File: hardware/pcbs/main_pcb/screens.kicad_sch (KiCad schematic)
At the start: 22 parts, among them J1 Conn_01x02, J2 Conn_01x07, J3 Conn_01x07, J4 Conn_01x13, U1 TXB0104D, U2 TXB0104D, U3 TXB0104D

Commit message: feat(main PCB): Reworks schematic
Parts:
- C1, C2, C3, C4, C5, C6, C7, C8, C9: symbol Device:C -> Lilybrary:Capacitor
- J1: symbol Connector_Generic:Conn_01x02 -> Lilybrary:Conn_01x02
- J2, J3: symbol Connector_Generic:Conn_01x07 -> Lilybrary:Conn_01x07
- J4: symbol Connector_Generic:Conn_01x13 -> Lilybrary:Conn_01x13
- R1: symbol Device:R -> Lilybrary:Resistor
- TP1, TP2, TP3, TP4, TP5: symbol Connector:TestPoint -> Lilybrary:TestPoint
- U1, U2, U3: footprint Package_SO:SOIC-14_3.9x8.7mm_P1.27mm -> Lilibrary:SOIC-14_TXB0104DR; symbol Logic_LevelTranslator:TXB0104D -> Lilybrary:TXB0104DR
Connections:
- net LEFT_EYE_CS-3V3: now also TP1. (1); no longer TP1.1
- net MAIN_SCREEN_CS-3V3: now also TP5. (1); no longer TP5.1
- net MISO_3V3: now also U2.5 (A4); no longer U2.3 (A2)
- net RIGHT_EYE_CS-3V3: now also TP2. (1); no longer TP2.1
- net SCK_3V3: now also U2.3 (A2); no longer U2.2 (A1)
- net SD_CS-3V3: now also TP4. (1); no longer TP4.1
- net DC-3V3 renamed DC_3V3
- net DC_3V3: now also TP3. (1), U2.2 (A1); no longer TP3.1, U2.5 (A4)
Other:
- company: (none) -> Lily's Pad
- title: (none) -> Main PCB: Screens
- moved on the sheet: J1, J2, J3, J4, TP3

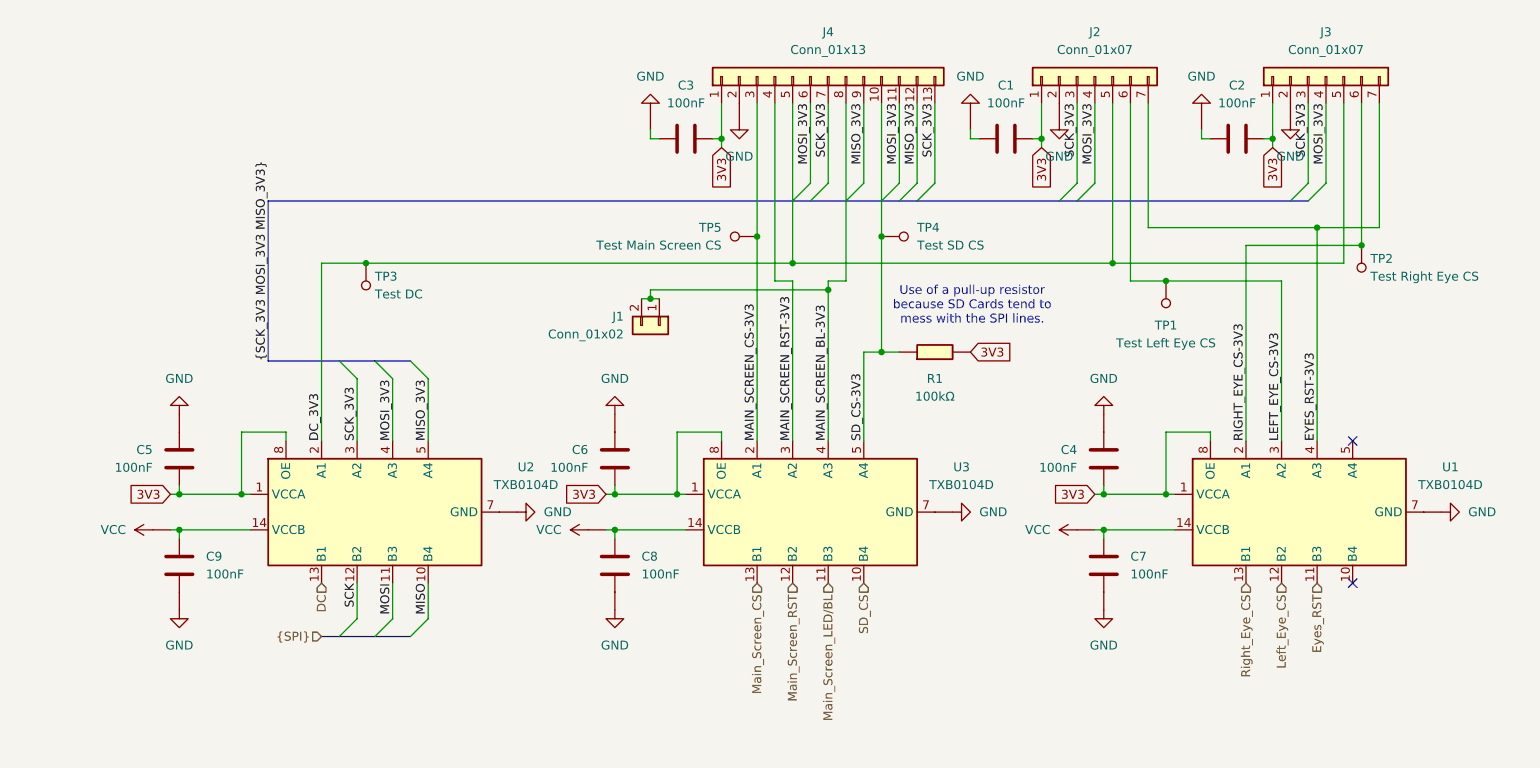
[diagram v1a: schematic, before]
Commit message: feat(main PCB): Removes no longer used BL pin 01x02 header
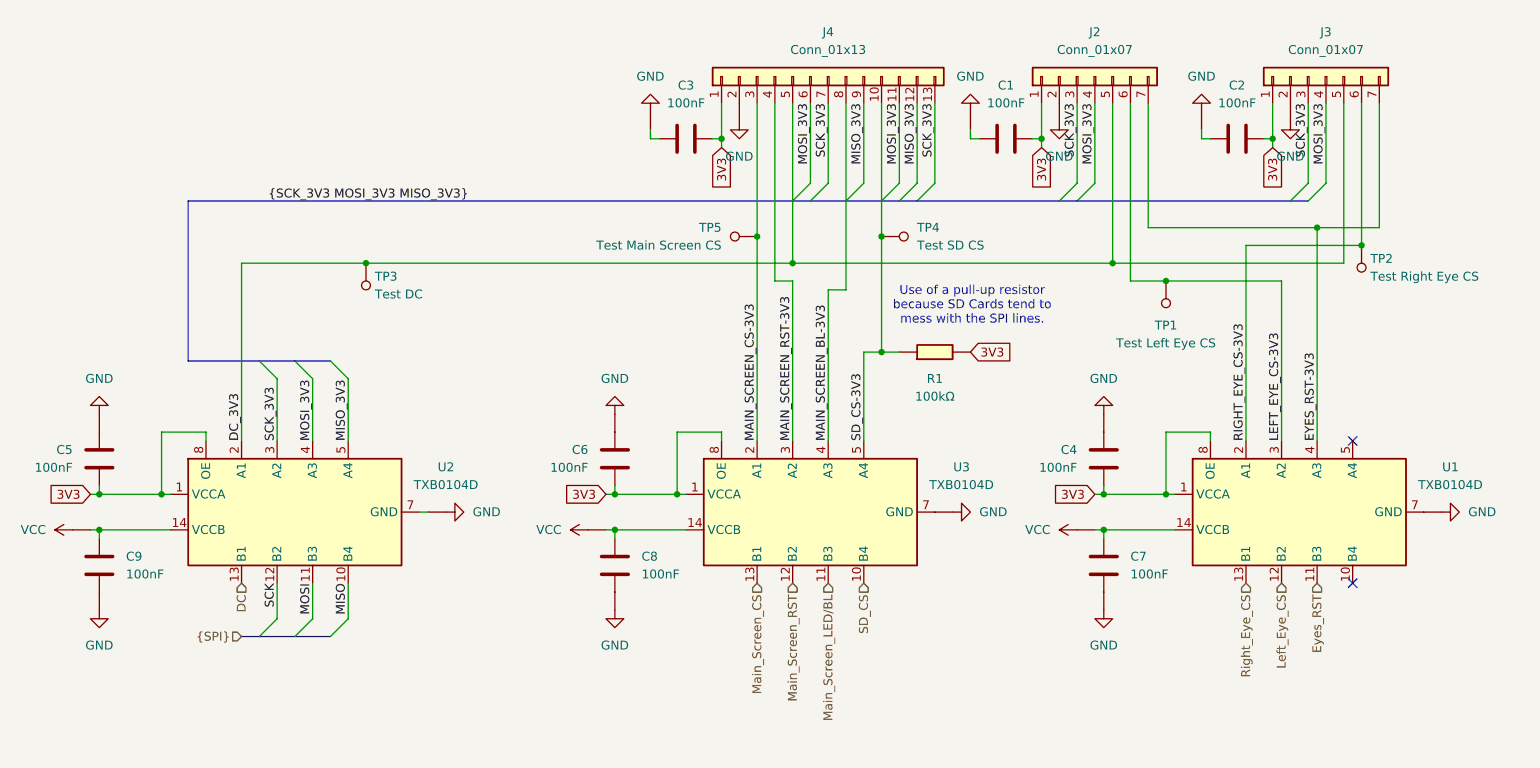
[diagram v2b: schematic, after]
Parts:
- removed J1: Conn_01x02, Lilibrary:JST XH 2 pins, symbol Lilybrary:Conn_01x02
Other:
- moved on the sheet: C5, C9, U2

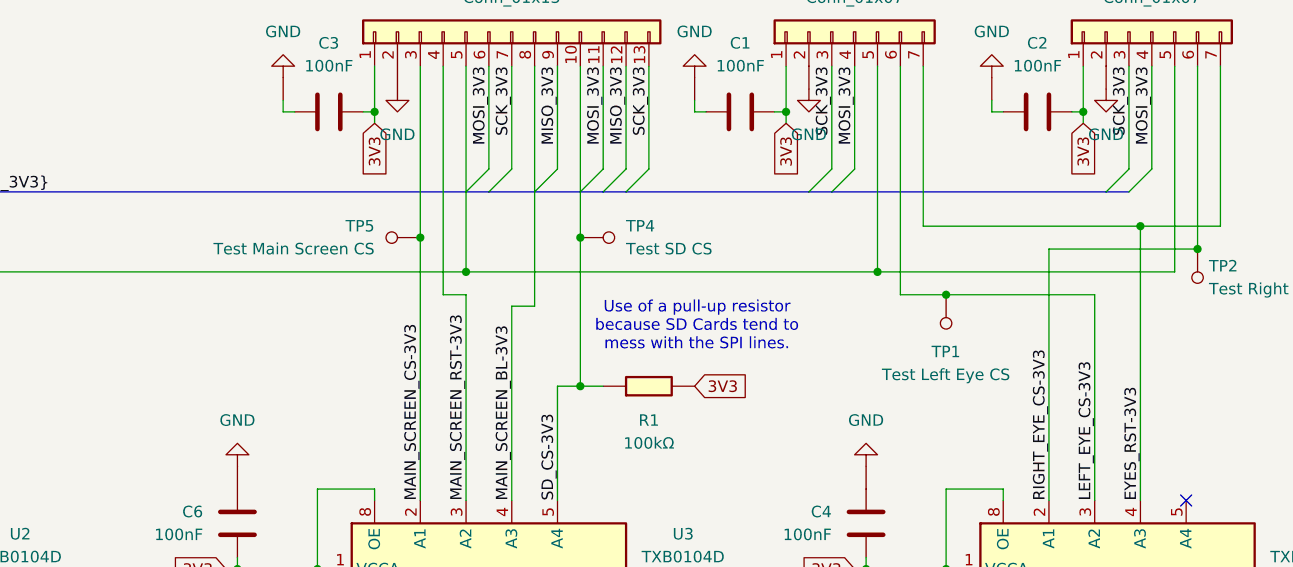
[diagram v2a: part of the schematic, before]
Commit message: feat(main PCB): Fixes main PCB routing issue
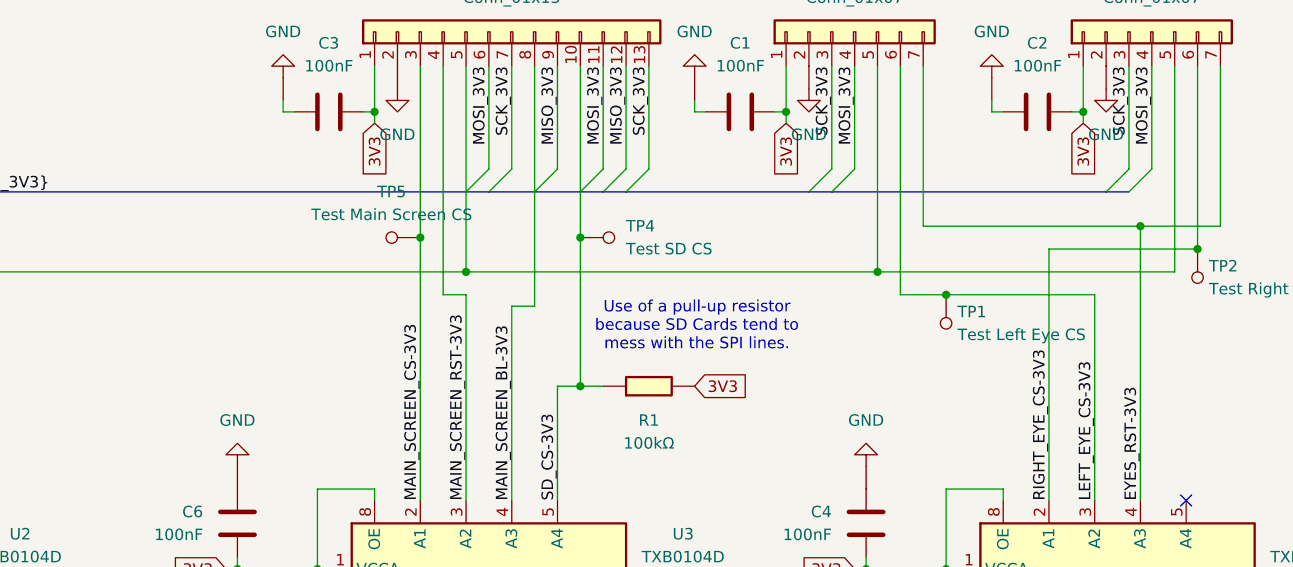
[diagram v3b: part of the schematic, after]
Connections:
- net DC_3V3: now also TP3.1; no longer TP3. (1)
- net LEFT_EYE_CS-3V3: now also TP1.1; no longer TP1. (1)
- net MAIN_SCREEN_CS-3V3: now also TP5.1; no longer TP5. (1)
- net RIGHT_EYE_CS-3V3: now also TP2.1; no longer TP2. (1)
- net SD_CS-3V3: now also TP4.1; no longer TP4. (1)
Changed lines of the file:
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@@
 			)
 		)
-		(pin ""
+		(pin "1"
 		)
 		(instances
@@
 			)
 		)
-		(pin ""
+		(pin "1"
 		)
 		(instances
@@
 			)
 		)
-		(pin ""
+		(pin "1"
 		)
 		(instances
@@
 		(fields_autoplaced yes)
 		(property "Reference" "TP1"
-			(at 199.39 90.17 0)
-			(effects
-				(font
-					(size 1.27 1.27)
-				)
+			(at 200.66 85.7249 0)
+			(effects
+				(font
+					(size 1.27 1.27)
+				)
+				(justify right)
 			)
 		)
 		(property "Value" "Test Left Eye CS"
-			(at 199.39 92.71 0)
-			(effects
-				(font
-					(size 1.27 1.27)
-				)
+			(at 200.66 88.2649 0)
+			(effects
+				(font
+					(size 1.27 1.27)
+				)
+				(justify right)
 			)
 		)
@@
 			)
 		)
-		(pin ""
+		(pin "1"
 		)
 		(instances
@@
 		(fields_autoplaced yes)
 		(property "Reference" "TP5"
-			(at 135.89 76.1999 90)
-			(effects
-				(font
-					(size 1.27 1.27)
-				)
-				(justify left)
+			(at 137.795 72.39 90)
+			(effects
+				(font
+					(size 1.27 1.27)
+				)
 			)
 		)
 		(property "Value" "Test Main Screen CS"
-			(at 135.89 78.7399 90)
-			(effects
-				(font
-					(size 1.27 1.27)
-				)
-				(justify left)
+			(at 137.795 74.93 90)
+			(effects
+				(font
+					(size 1.27 1.27)
+				)
 			)
 		)
@@
 			)
 		)
-		(pin ""
-		)
-		(instances
+		(pin "1"
+		)
+		(instances
